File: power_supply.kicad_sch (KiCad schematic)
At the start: 30 parts

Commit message: Organizado a folha da power supply
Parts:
- removed C10: (no value), symbol Device:C
- added C11: (no value), Capacitor_SMD:C_1206_3216Metric_Pad1.33x1.80mm_HandSolder, symbol Device:C
- added C3: 100nF, Capacitor_SMD:C_0402_1005Metric_Pad0.74x0.62mm_HandSolder, symbol Device:C
- C1: value (none) -> 10nF; footprint (none) -> Capacitor_SMD:C_0402_1005Metric_Pad0.74x0.62mm_HandSolder
- C4: renamed from C3; value (none) -> 22uF/16V; footprint (none) -> Capacitor_SMD:C_1206_3216Metric_Pad1.33x1.80mm_HandSolder
- C5: renamed from C4; value (none) -> 22uF/16V; footprint (none) -> Capacitor_SMD:C_1206_3216Metric_Pad1.33x1.80mm_HandSolder
- C6: renamed from C7; value (none) -> 6,8nF; footprint (none) -> Capacitor_SMD:C_0402_1005Metric_Pad0.74x0.62mm_HandSolder
- C7: renamed from C8; value (none) -> 100nF; footprint (none) -> Capacitor_SMD:C_0402_1005Metric_Pad0.74x0.62mm_HandSolder
- C8: renamed from C5; footprint (none) -> Capacitor_SMD:C_1206_3216Metric_Pad1.33x1.80mm_HandSolder
- C9: renamed from C6; footprint (none) -> Capacitor_SMD:C_0402_1005Metric_Pad0.74x0.62mm_HandSolder
- CON1: renamed from CON2; value (none) -> USB_B_Micro; footprint (none) -> Connector_USB:USB_Micro-B_GCT_USB3076-30-A
- CON2: renamed from CON1; value (none) -> Barrel_Jack_MountingPin; footprint (none) -> Connector_BarrelJack:BarrelJack_GCT_DCJ200-10-A_Horizontal
- D1: renamed from D2; value (none) -> BAT60A; footprint (none) -> Diode_SMD:D_SOD-323
- D2: renamed from D1; value (none) -> BAT60A; footprint (none) -> Diode_SMD:D_SOD-323
- L1: value (none) -> 10uH; footprint (none) -> Inductor_SMD:L_Bourns-SRN8040_8x8.15mm
- Q1: value (none) -> AO3401A; footprint (none) -> Package_TO_SOT_SMD:SOT-23
- R1: renamed from R4; value (none) -> 1k
- R10: renamed from R5; value (none) -> 6k8
- R11: value (none) -> 100k; footprint (none) -> Resistor_SMD:R_0402_1005Metric_Pad0.72x0.64mm_HandSolder
- R12: value (none) -> 100k
- R2: renamed from R6; value (none) -> 0R; footprint (none) -> Resistor_SMD:R_0402_1005Metric_Pad0.72x0.64mm_HandSolder
- R3: renamed from R7; value (none) -> 0R; footprint (none) -> Resistor_SMD:R_0402_1005Metric_Pad0.72x0.64mm_HandSolder
- R4: renamed from R8; value (none) -> 22k
- R5: renamed from R1; value (none) -> 100k; footprint (none) -> Resistor_SMD:R_0402_1005Metric_Pad0.72x0.64mm_HandSolder
- R6: renamed from R2; value (none) -> 26k1
- R7: renamed from R9; value (none) -> 47k
- R8: renamed from R10; value (none) -> 10k
- R9: renamed from R3; value (none) -> 10k
- U1: value (none) -> AP6503
- U2: value (none) -> CP2102N; footprint (none) -> Package_DFN_QFN:QFN-28-1EP_5x5mm_P0.5mm_EP3.35x3.35mm
- renumbered C9 to C10
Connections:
- net GNDREF: now also C11.2, C3.1
- net VCC: now also C11.1, C3.2
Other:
- note added: "MICRO USB +5V"
- note added: "POWER SELECT"
- note added: "POWER SUPPLY (5V~12V to 3.3V)"
- note added: "USB-UART"
- note removed: "+5V/+12V P/ +3.3V"
- note removed: "USB +5V"
- moved on the sheet: C1, C10, C2, C4, C5, C6, C7, C8, C9, CON1, CON2, D1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

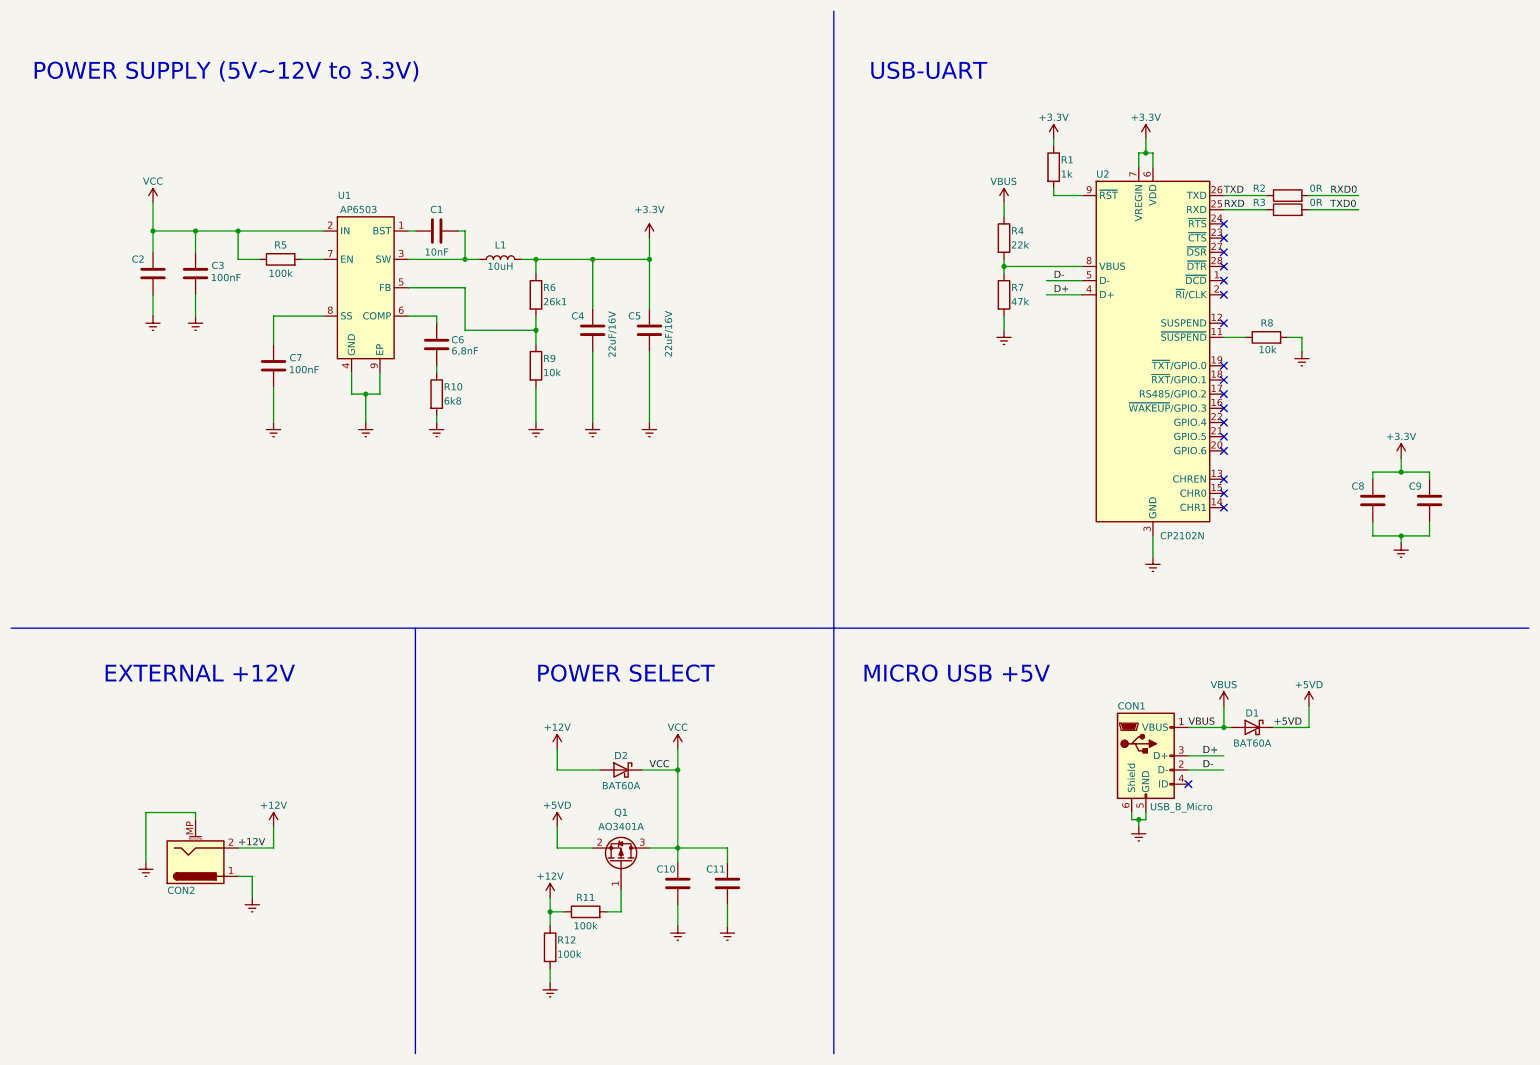
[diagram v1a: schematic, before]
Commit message: Iniciando o circuito do PHY Ethernet
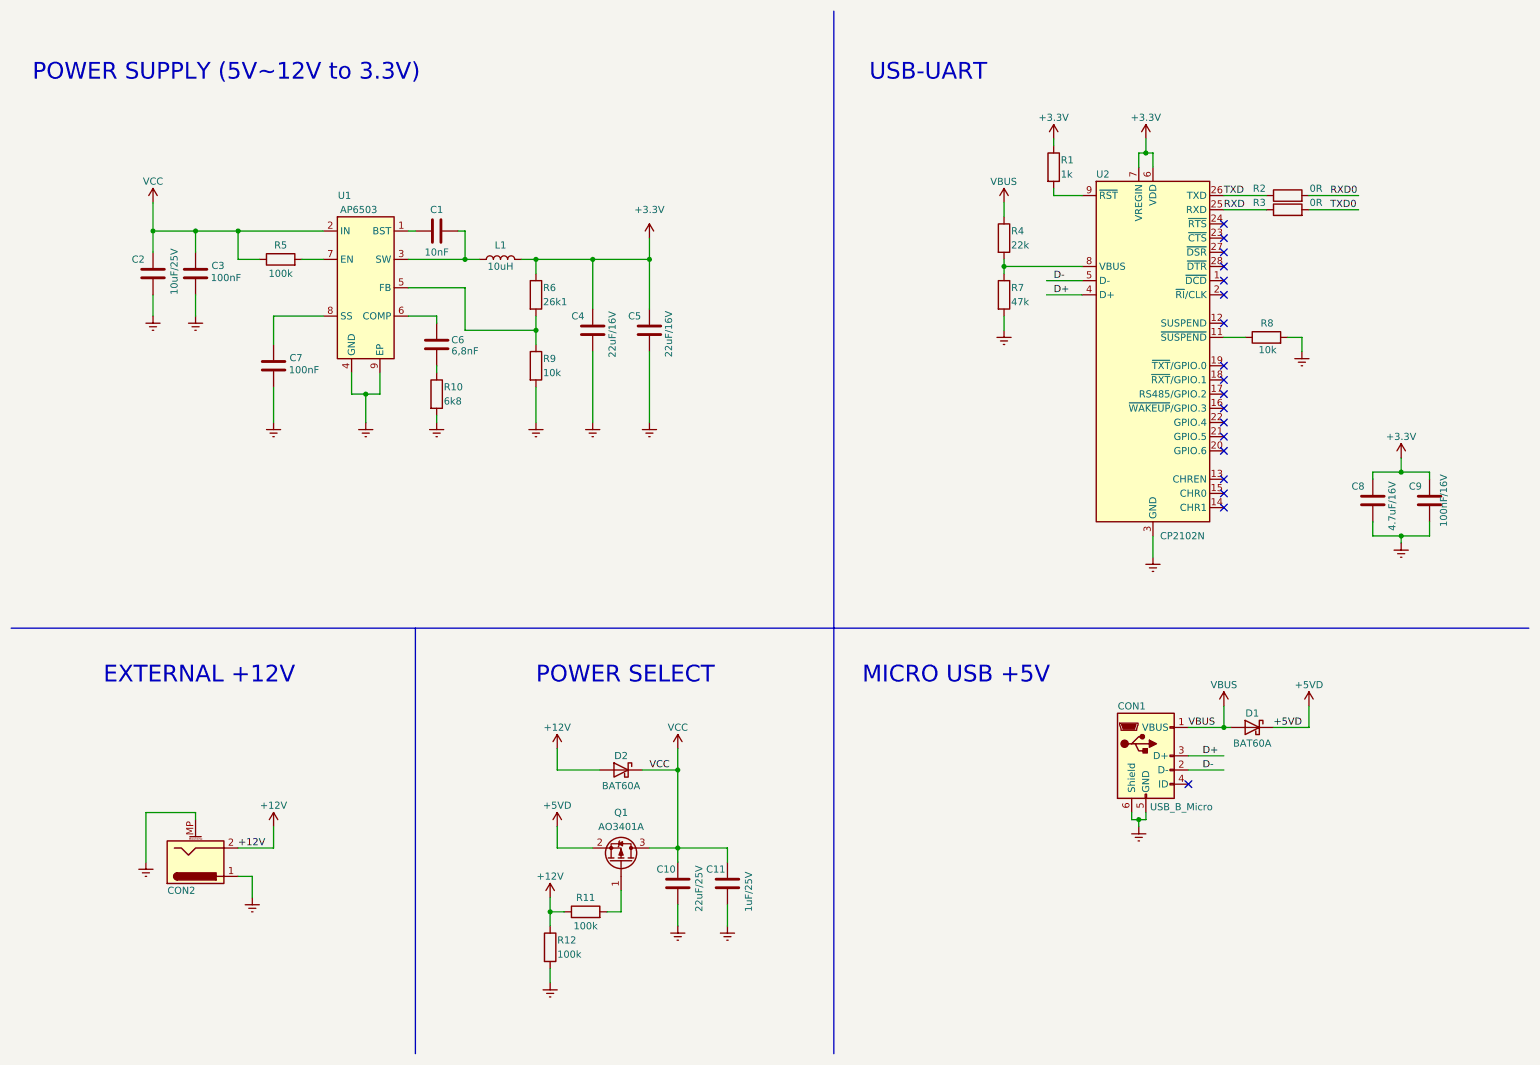
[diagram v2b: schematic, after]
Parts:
- C10: value (none) -> 22uF/25V; footprint (none) -> Capacitor_SMD:C_1206_3216Metric_Pad1.33x1.80mm_HandSolder
- C11: value (none) -> 1uF/25V
- C2: value (none) -> 10uF/25V; footprint (none) -> Capacitor_SMD:C_1206_3216Metric_Pad1.33x1.80mm_HandSolder
- C8: value (none) -> 4.7uF/16V
- C9: value (none) -> 100nF/16V
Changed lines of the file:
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@@
       (effects (font (size 1.27 1.27)) (justify left))
     )
-    (property "Value" "" (id 1) (at 144.78 172.72 90)
+    (property "Value" "1uF/25V" (id 1) (at 144.78 172.72 90)
       (effects (font (size 1.27 1.27)) (justify left))
     )
@@
     (in_bom yes) (on_board yes)
     (property "Reference" "C9" (id 0) (at 264.16 96.52 0))
-    (property "Value" "" (id 1) (at 269.24 99.06 90))
+    (property "Value" "100nF/16V" (id 1) (at 269.24 99.06 90))
     (property "Footprint" "Capacitor_SMD:C_0402_1005Metric_Pad0.74x0.62mm_HandSolder" (id 2) (at 265.7348 95.25 0)
       (effects (font (size 1.27 1.27)) hide)
@@
       (effects (font (size 1.27 1.27)) (justify left))
     )
-    (property "Value" "" (id 1) (at 135.89 172.72 90)
-      (effects (font (size 1.27 1.27)) (justify left))
-    )
-    (property "Footprint" "" (id 2) (at 133.0452 171.45 0)
+    (property "Value" "22uF/25V" (id 1) (at 135.89 172.72 90)
+      (effects (font (size 1.27 1.27)) (justify left))
+    )
+    (property "Footprint" "Capacitor_SMD:C_1206_3216Metric_Pad1.33x1.80mm_HandSolder" (id 2) (at 133.0452 171.45 0)
       (effects (font (size 1.27 1.27)) hide)
     )
@@
       (effects (font (size 1.27 1.27)) (justify left))
     )
-    (property "Value" "" (id 1) (at 41.91 62.23 90)
-      (effects (font (size 1.27 1.27)) (justify left))
-    )
-    (property "Footprint" "" (id 2) (at 39.0652 62.23 0)
+    (property "Value" "10uF/25V" (id 1) (at 41.91 62.23 90)
+      (effects (font (size 1.27 1.27)) (justify left))
+    )
+    (property "Footprint" "Capacitor_SMD:C_1206_3216Metric_Pad1.33x1.80mm_HandSolder" (id 2) (at 39.0652 62.23 0)
       (effects (font (size 1.27 1.27)) hide)
     )
@@
       (effects (font (size 1.27 1.27)) (justify left))
     )
-    (property "Value" "" (id 1) (at 260.0068 104.4817 90)
-      (effects (font (size 1.27 1.27)) (justify left))
-    )
+    (property "Value" "4.7uF/16V" (id 1) (at 260.0068 104.4817 90)
+      (effects (font (size 1.27 1.27)) (justify left))
+    )

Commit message: Continuando o circuito do PHY Ethernet
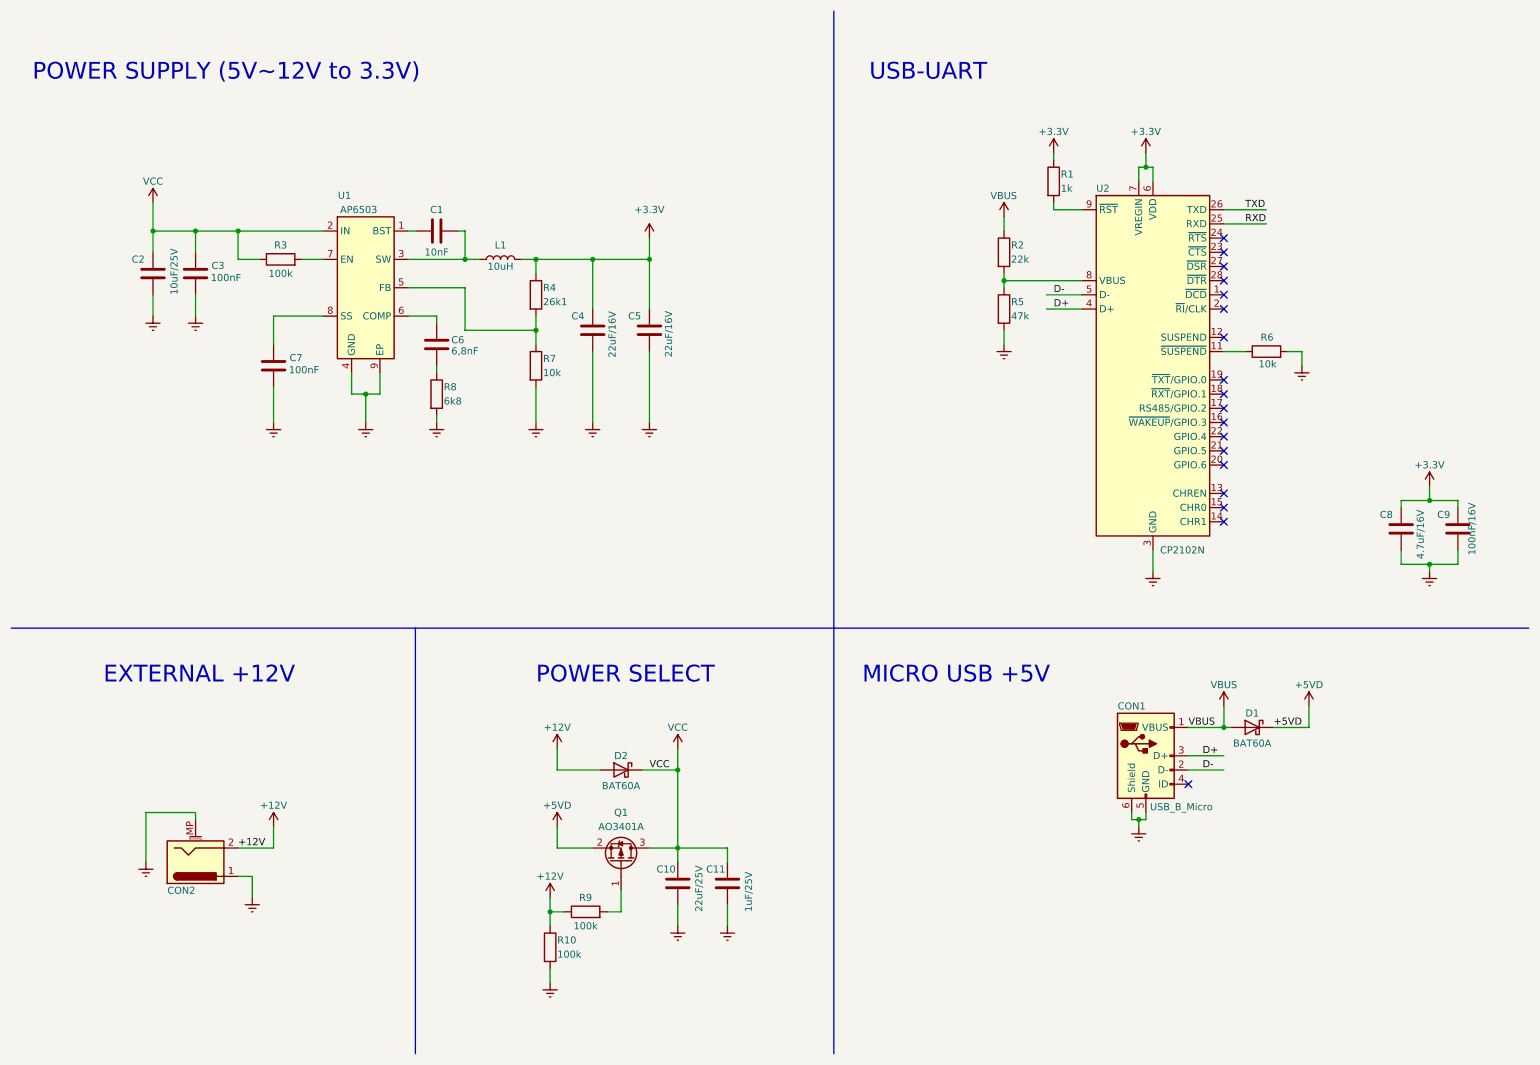
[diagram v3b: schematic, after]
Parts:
- removed R2, R3: 0R, Resistor_SMD:R_0402_1005Metric_Pad0.72x0.64mm_HandSolder, symbol Device:R
- renumbered R12 to R10, R4 to R2, R5 to R3, R6 to R4, R7 to R5, R8 to R6, R9 to R7, R10 to R8, R11 to R9
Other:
- moved on the sheet: C8, C9, R1, R2, R5, R6, U2

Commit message: Concluido o circuito do PHY ETH
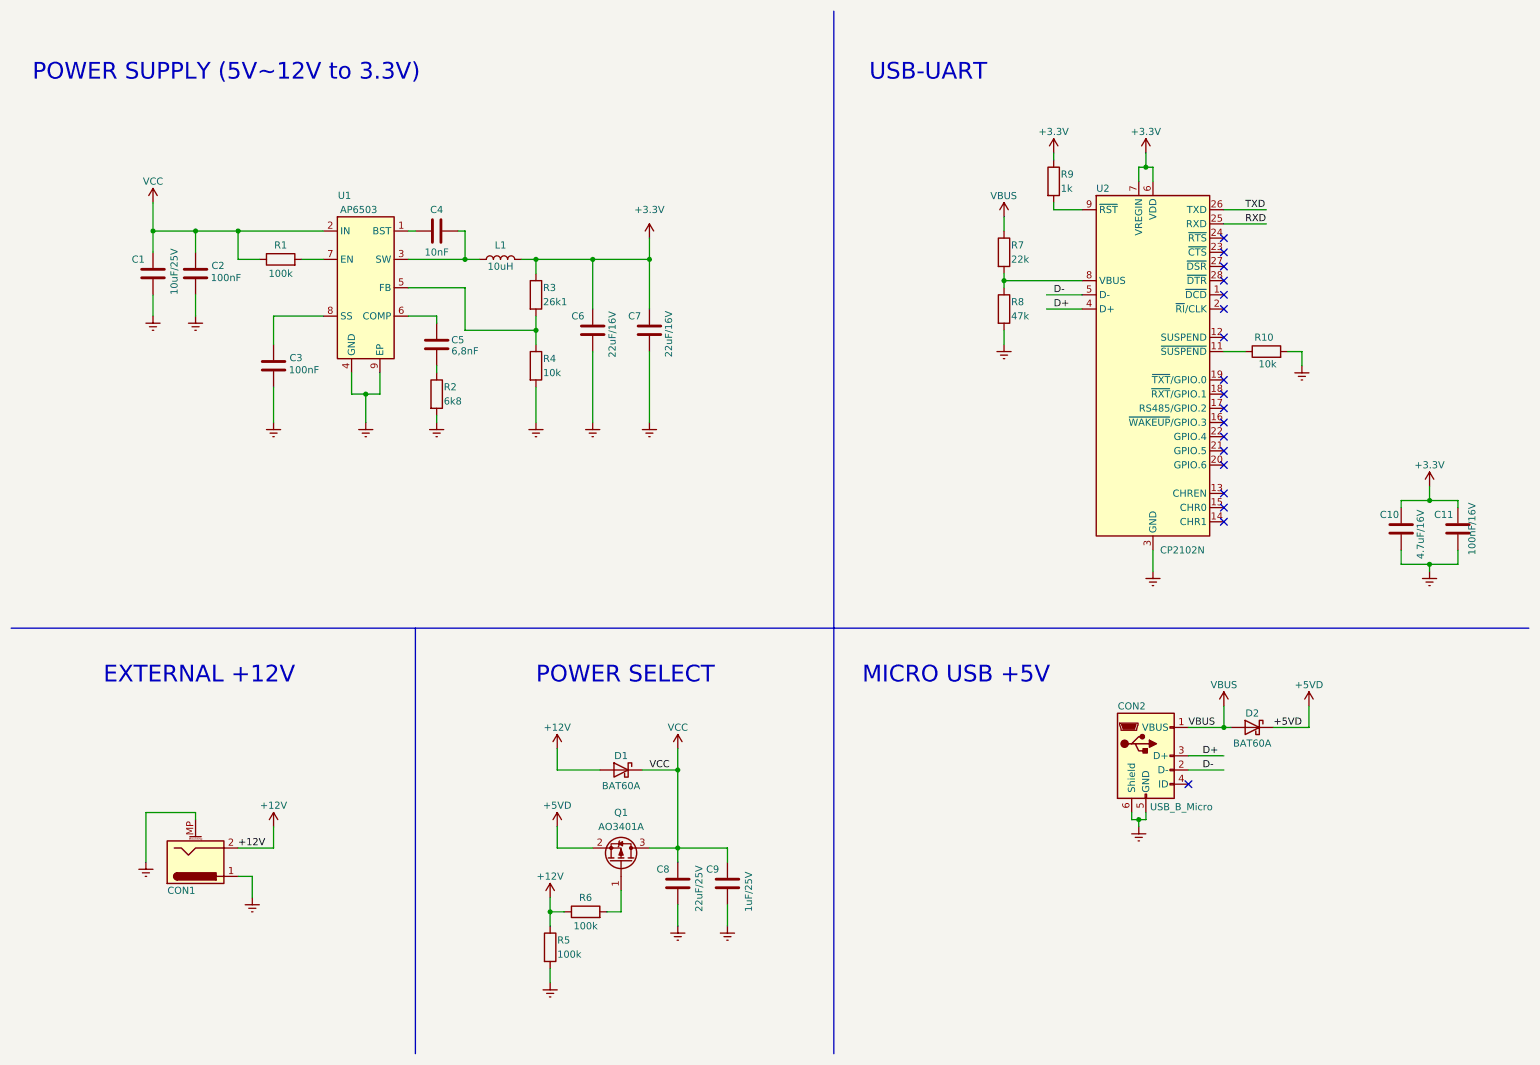
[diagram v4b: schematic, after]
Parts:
- renumbered C2 to C1, C8 to C10, C9 to C11, C3 to C2, C7 to C3, C1 to C4, C6 to C5, C4 to C6, C5 to C7, C10 to C8, C11 to C9, CON2 to CON1, CON1 to CON2, D2 to D1, D1 to D2, R3 to R1, R6 to R10, R8 to R2, R4 to R3, R7 to R4, R10 to R5, R9 to R6, R2 to R7, R5 to R8, R1 to R9

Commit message: Adicionado o circuito de entrada do PHY ETH
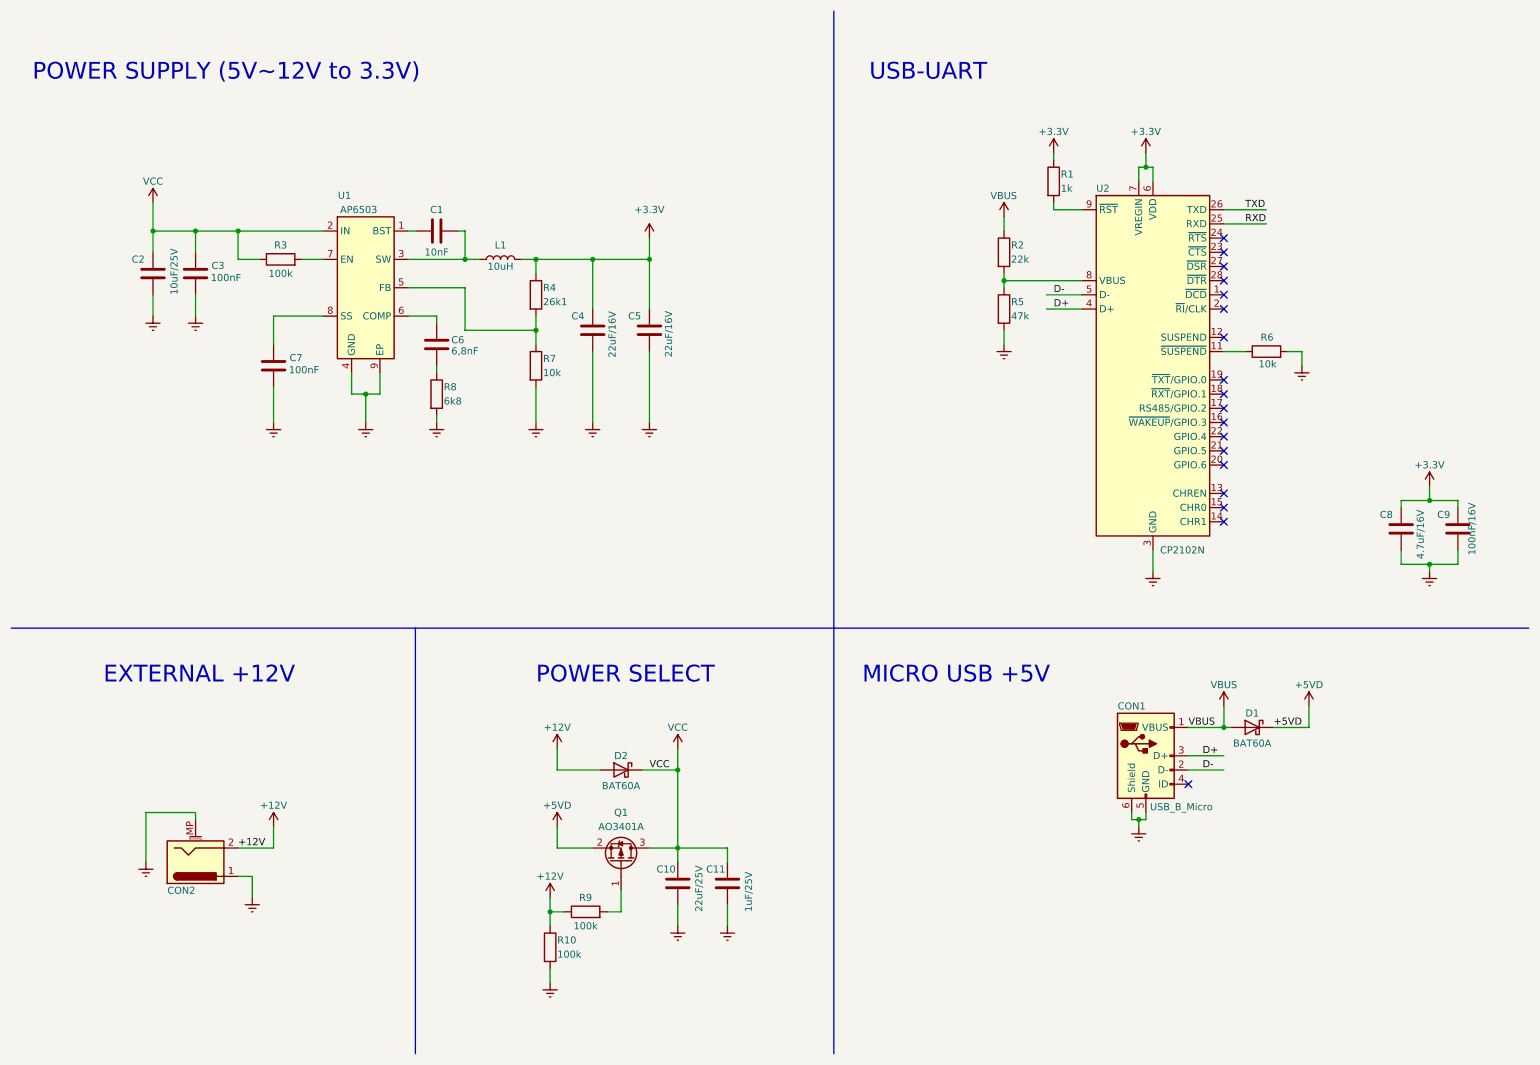
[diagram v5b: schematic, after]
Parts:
- renumbered C4 to C1, C8 to C10, C9 to C11, C1 to C2, C2 to C3, C6 to C4, C7 to C5, C5 to C6, C3 to C7, C10 to C8, C11 to C9, CON2 to CON1, CON1 to CON2, D2 to D1, D1 to D2, R9 to R1, R5 to R10, R7 to R2, R1 to R3, R3 to R4, R8 to R5, R10 to R6, R4 to R7, R2 to R8, R6 to R9
